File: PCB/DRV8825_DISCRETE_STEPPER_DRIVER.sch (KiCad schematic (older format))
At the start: 14 parts, among them U4 DRV8825PWPR

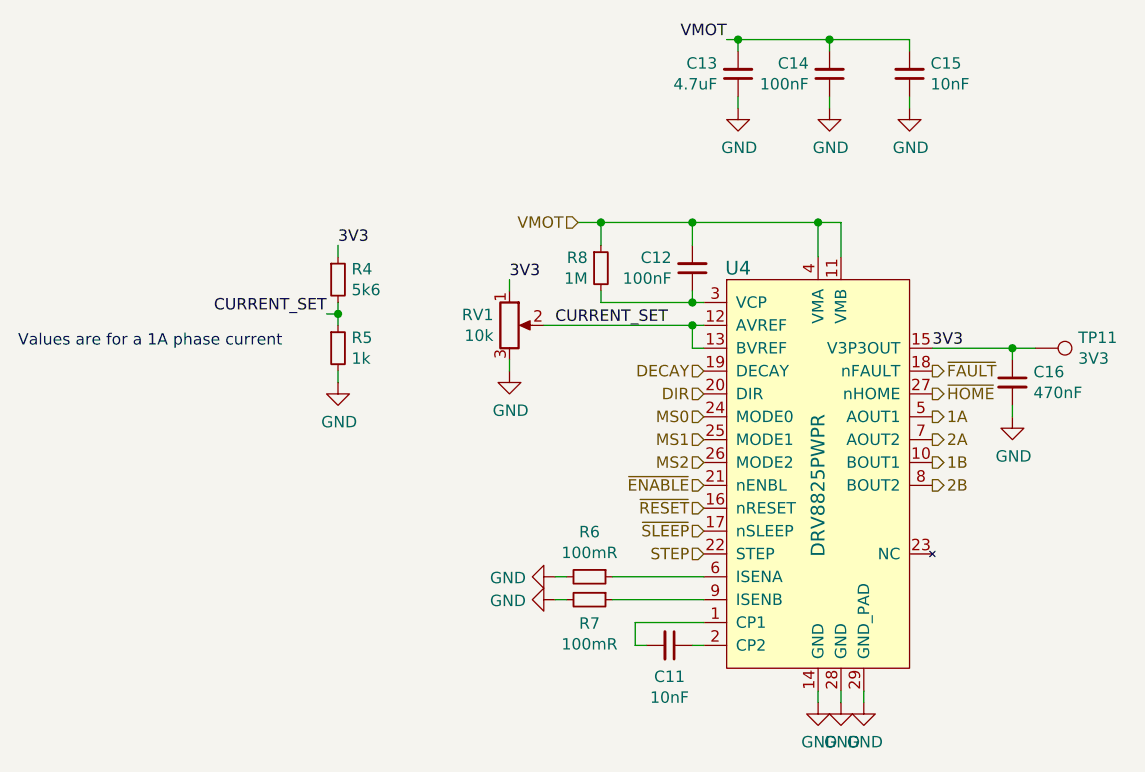
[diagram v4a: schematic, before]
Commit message: Added PDF schematic
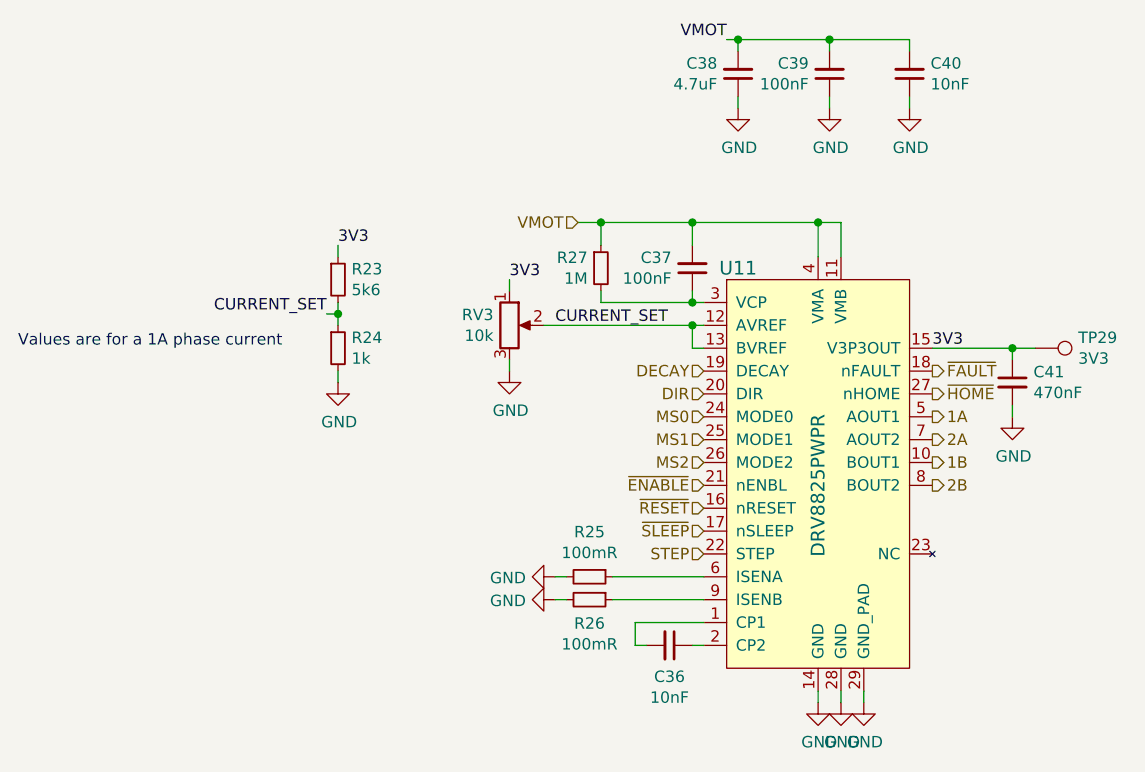
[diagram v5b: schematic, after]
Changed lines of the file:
@@
 AR Path="/5E8A6686/5E8D27A6/5E8D3351" Ref="U4"  Part="1"
 AR Path="/5E8813FF/5E8D27A6/5E8D3351" Ref="U11"  Part="1"
-F 0 "U4" H 5300 4500 60  0000 C CNN
+F 0 "U11" H 5300 4500 60  0000 C CNN
 F 1 "DRV8825PWPR" V 5650 3550 60  0000 C CNN
 F 2 "digikey-footprints:TSSOP-28-1EP_W4.40mm" H 5750 4050 60  0001 L CNN
@@
 AR Path="/5E8A6686/5E8D27A6/5E8D575F" Ref="C11"  Part="1"
 AR Path="/5E8813FF/5E8D27A6/5E8D575F" Ref="C36"  Part="1"
-F 0 "C11" V 5137 4850 50  0000 C CNN
+F 0 "C36" V 5137 4850 50  0000 C CNN
 F 1 "10nF" V 5228 4850 50  0000 C CNN
 F 2 "" H 5000 4850 50  0001 C CNN
@@
 AR Path="/5E8A6686/5E8D27A6/5E8D7A25" Ref="R6"  Part="1"
 AR Path="/5E8813FF/5E8D27A6/5E8D7A25" Ref="R25"  Part="1"
-F 0 "R6" V 4454 4550 50  0000 C CNN
+F 0 "R25" V 4454 4550 50  0000 C CNN
 F 1 "100mR" V 4545 4550 50  0000 C CNN
 F 2 "" H 4650 4550 50  0001 C CNN
@@
 AR Path="/5E8A6686/5E8D27A6/5E8D7F7E" Ref="R7"  Part="1"
 AR Path="/5E8813FF/5E8D27A6/5E8D7F7E" Ref="R26"  Part="1"
-F 0 "R7" V 4754 4650 50  0000 C CNN
+F 0 "R26" V 4754 4650 50  0000 C CNN
 F 1 "100mR" V 4845 4650 50  0000 C CNN
 F 2 "" H 4650 4650 50  0001 C CNN
@@
 AR Path="/5E8A6686/5E8D27A6/5E8D91C5" Ref="#PWR041"  Part="1"
 AR Path="/5E8813FF/5E8D27A6/5E8D91C5" Ref="#PWR0106"  Part="1"
-F 0 "#PWR041" H 4500 4300 50  0001 C CNN
+F 0 "#PWR0106" H 4500 4300 50  0001 C CNN
 F 1 "GND" V 4505 4422 50  0000 R CNN
 F 2 "" H 4500 4550 50  0001 C CNN
@@
 AR Path="/5E8A6686/5E8D27A6/5E8D92EE" Ref="#PWR042"  Part="1"
 AR Path="/5E8813FF/5E8D27A6/5E8D92EE" Ref="#PWR0107"  Part="1"
-F 0 "#PWR042" H 4500 4400 50  0001 C CNN
+F 0 "#PWR0107" H 4500 4400 50  0001 C CNN
 F 1 "GND" V 4505 4522 50  0000 R CNN
 F 2 "" H 4500 4650 50  0001 C CNN
@@
 AR Path="/5E8A6686/5E8D27A6/5E8DA337" Ref="C12"  Part="1"
 AR Path="/5E8813FF/5E8D27A6/5E8DA337" Ref="C37"  Part="1"
-F 0 "C12" H 5191 3154 50  0000 L CNN
+F 0 "C37" H 5191 3154 50  0000 L CNN
 F 1 "100nF" H 5191 3245 50  0000 L CNN
 F 2 "" H 5100 3200 50  0001 C CNN
@@
 AR Path="/5E8A6686/5E8D27A6/5E8DF1FC" Ref="RV1"  Part="1"
 AR Path="/5E8813FF/5E8D27A6/5E8DF1FC" Ref="RV3"  Part="1"
-F 0 "RV1" H 4230 3496 50  0000 R CNN
+F 0 "RV3" H 4230 3496 50  0000 R CNN
 F 1 "10k" H 4230 3405 50  0000 R CNN
 F 2 "" H 4300 3450 50  0001 C CNN
@@
 AR Path="/5E8A6686/5E8D27A6/5E8E02D7" Ref="#PWR040"  Part="1"
 AR Path="/5E8813FF/5E8D27A6/5E8E02D7" Ref="#PWR0105"  Part="1"
-F 0 "#PWR040" H 4300 3400 50  0001 C CNN
+F 0 "#PWR0105" H 4300 3400 50  0001 C CNN
 F 1 "GND" H 4305 3477 50  0000 C CNN
 F 2 "" H 4300 3650 50  0001 C CNN
@@
 AR Path="/5E8A6686/5E8D27A6/5E8E181B" Ref="C16"  Part="1"
 AR Path="/5E8813FF/5E8D27A6/5E8E181B" Ref="C41"  Part="1"
-F 0 "C16" H 6592 3746 50  0000 L CNN
+F 0 "C41" H 6592 3746 50  0000 L CNN
 F 1 "470nF" H 6592 3655 50  0000 L CNN
 F 2 "" H 6500 3700 50  0001 C CNN
@@
 AR Path="/5E8A6686/5E8D27A6/5E8E24E3" Ref="#PWR049"  Part="1"
 AR Path="/5E8813FF/5E8D27A6/5E8E24E3" Ref="#PWR0114"  Part="1"
-F 0 "#PWR049" H 6500 3600 50  0001 C CNN
+F 0 "#PWR0114" H 6500 3600 50  0001 C CNN
 F 1 "GND" H 6505 3677 50  0000 C CNN
 F 2 "" H 6500 3850 50  0001 C CNN
@@
 AR Path="/5E8A6686/5E8D27A6/5E8E69E3" Ref="#PWR044"  Part="1"
 AR Path="/5E8813FF/5E8D27A6/5E8E69E3" Ref="#PWR0109"  Part="1"
-F 0 "#PWR044" H 5650 4850 50  0001 C CNN
+F 0 "#PWR0109" H 5650 4850 50  0001 C CNN
 F 1 "GND" H 5655 4927 50  0000 C CNN
 F 2 "" H 5650 5100 50  0001 C CNN
@@
 AR Path="/5E8A6686/5E8D27A6/5E8E6E0E" Ref="#PWR046"  Part="1"
 AR Path="/5E8813FF/5E8D27A6/5E8E6E0E" Ref="#PWR0111"  Part="1"
-F 0 "#PWR046" H 5750 4850 50  0001 C CNN
+F 0 "#PWR0111" H 5750 4850 50  0001 C CNN
 F 1 "GND" H 5755 4927 50  0000 C CNN
 F 2 "" H 5750 5100 50  0001 C CNN
@@
 AR Path="/5E8A6686/5E8D27A6/5E8E6F63" Ref="#PWR047"  Part="1"
 AR Path="/5E8813FF/5E8D27A6/5E8E6F63" Ref="#PWR0112"  Part="1"
-F 0 "#PWR047" H 5850 4850 50  0001 C CNN
+F 0 "#PWR0112" H 5850 4850 50  0001 C CNN
 F 1 "GND" H 5855 4927 50  0000 C CNN
 F 2 "" H 5850 5100 50  0001 C CNN
@@
 AR Path="/5E8A6686/5E8D27A6/5E8E9760" Ref="C13"  Part="1"
 AR Path="/5E8813FF/5E8D27A6/5E8E9760" Ref="C38"  Part="1"
-F 0 "C13" H 5391 2304 50  0000 L CNN
+F 0 "C38" H 5391 2304 50  0000 L CNN
 F 1 "4.7uF" H 5391 2395 50  0000 L CNN
 F 2 "" H 5300 2350 50  0001 C CNN
@@
 AR Path="/5E8A6686/5E8D27A6/5E8E999E" Ref="C14"  Part="1"
 AR Path="/5E8813FF/5E8D27A6/5E8E999E" Ref="C39"  Part="1"
-F 0 "C14" H 5791 2304 50  0000 L CNN
+F 0 "C39" H 5791 2304 50  0000 L CNN
 F 1 "100nF" H 5791 2395 50  0000 L CNN
 F 2 "" H 5700 2350 50  0001 C CNN
@@
 AR Path="/5E8A6686/5E8D27A6/5E8E9DB5" Ref="C15"  Part="1"
 AR Path="/5E8813FF/5E8D27A6/5E8E9DB5" Ref="C40"  Part="1"
-F 0 "C15" H 5958 2304 50  0000 R CNN
+F 0 "C40" H 5958 2304 50  0000 R CNN
 F 1 "10nF" H 5958 2395 50  0000 R CNN
 F 2 "" H 6050 2350 50  0001 C CNN
@@
 AR Path="/5E8A6686/5E8D27A6/5E8F0245" Ref="#PWR043"  Part="1"
 AR Path="/5E8813FF/5E8D27A6/5E8F0245" Ref="#PWR0108"  Part="1"
-F 0 "#PWR043" H 5300 2250 50  0001 C CNN
+F 0 "#PWR0108" H 5300 2250 50  0001 C CNN
 F 1 "GND" H 5305 2327 50  0000 C CNN
 F 2 "" H 5300 2500 50  0001 C CNN
@@
 AR Path="/5E8A6686/5E8D27A6/5E8F04AF" Ref="#PWR045"  Part="1"
 AR Path="/5E8813FF/5E8D27A6/5E8F04AF" Ref="#PWR0110"  Part="1"
-F 0 "#PWR045" H 5700 2250 50  0001 C CNN
+F 0 "#PWR0110" H 5700 2250 50  0001 C CNN
 F 1 "GND" H 5705 2327 50  0000 C CNN
 F 2 "" H 5700 2500 50  0001 C CNN
@@
 AR Path="/5E8A6686/5E8D27A6/5E8F06A3" Ref="#PWR048"  Part="1"
 AR Path="/5E8813FF/5E8D27A6/5E8F06A3" Ref="#PWR0113"  Part="1"
-F 0 "#PWR048" H 6050 2250 50  0001 C CNN
+F 0 "#PWR0113" H 6050 2250 50  0001 C CNN
 F 1 "GND" H 6055 2327 50  0000 C CNN
 F 2 "" H 6050 2500 50  0001 C CNN
@@
 AR Path="/5E8A6686/5E8D27A6/5E8B797B" Ref="R4"  Part="1"
 AR Path="/5E8813FF/5E8D27A6/5E8B797B" Ref="R23"  Part="1"
-F 0 "R4" H 3609 3296 50  0000 L CNN
+F 0 "R23" H 3609 3296 50  0000 L CNN
 F 1 "5k6" H 3609 3205 50  0000 L CNN
 F 2 "" H 3550 3250 50  0001 C CNN
@@
 AR Path="/5E8A6686/5E8D27A6/5E8B7AF6" Ref="R5"  Part="1"
 AR Path="/5E8813FF/5E8D27A6/5E8B7AF6" Ref="R24"  Part="1"
-F 0 "R5" H 3609 3596 50  0000 L CNN
+F 0 "R24" H 3609 3596 50  0000 L CNN
 F 1 "1k" H 3609 3505 50  0000 L CNN
 F 2 "" H 3550 3550 50  0001 C CNN
@@
 AR Path="/5E8A6686/5E8D27A6/5E8B7CD9" Ref="#PWR039"  Part="1"
 AR Path="/5E8813FF/5E8D27A6/5E8B7CD9" Ref="#PWR0104"  Part="1"
-F 0 "#PWR039" H 3550 3450 50  0001 C CNN
+F 0 "#PWR0104" H 3550 3450 50  0001 C CNN
 F 1 "GND" H 3555 3527 50  0000 C CNN
 F 2 "" H 3550 3700 50  0001 C CNN
@@
 AR Path="/5E8A6686/5E8D27A6/5E8D6554" Ref="R8"  Part="1"
 AR Path="/5E8813FF/5E8D27A6/5E8D6554" Ref="R27"  Part="1"
-F 0 "R8" H 4642 3246 50  0000 R CNN
+F 0 "R27" H 4642 3246 50  0000 R CNN
 F 1 "1M" H 4642 3155 50  0000 R CNN
 F 2 "" H 4700 3200 50  0001 C CNN
@@
 AR Path="/5E8A6686/5E8D27A6/5E958C53" Ref="TP11"  Part="1"
 AR Path="/5E8813FF/5E8D27A6/5E958C53" Ref="TP29"  Part="1"
-F 0 "TP11" V 6554 3738 50  0000 L CNN
+F 0 "TP29" V 6554 3738 50  0000 L CNN
 F 1 "3V3" V 6645 3738 50  0000 L CNN
 F 2 "" H 6800 3550 50  0001 C CNN

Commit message: Added majority footprints
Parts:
- C11, C12, C13, C14, C15, C16: footprint (none) -> Capacitor_SMD:C_0603_1608Metric
- R4, R5, R8: footprint (none) -> Resistor_SMD:R_0603_1608Metric
- TP11: footprint (none) -> custom:TestPoint_Pad_D1.5mm
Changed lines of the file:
@@
 $Descr A4 11693 8268
 encoding utf-8
-Sheet 4 22
+Sheet 15 22
 Title ""
 Date ""
@@
 F 0 "C36" V 5137 4850 50  0000 C CNN
 F 1 "10nF" V 5228 4850 50  0000 C CNN
-F 2 "" H 5000 4850 50  0001 C CNN
+F 2 "Capacitor_SMD:C_0603_1608Metric" H 5000 4850 50  0001 C CNN
 F 3 "" H 5000 4850 50  0001 C CNN
 F 4 "X7R" H 5000 4850 50  0001 C CNN "Dielectric"
@@
 F 0 "C37" H 5191 3154 50  0000 L CNN
 F 1 "100nF" H 5191 3245 50  0000 L CNN
-F 2 "" H 5100 3200 50  0001 C CNN
+F 2 "Capacitor_SMD:C_0603_1608Metric" H 5100 3200 50  0001 C CNN
 F 3 "" H 5100 3200 50  0001 C CNN
 F 4 "X7R" H 5100 3200 50  0001 C CNN "Dielectric"
@@
 F 0 "C41" H 6592 3746 50  0000 L CNN
 F 1 "470nF" H 6592 3655 50  0000 L CNN
-F 2 "" H 6500 3700 50  0001 C CNN
+F 2 "Capacitor_SMD:C_0603_1608Metric" H 6500 3700 50  0001 C CNN
 F 3 "" H 6500 3700 50  0001 C CNN
 F 4 "X7R" H 6500 3700 50  0001 C CNN "Dielectric"
@@
 F 0 "C38" H 5391 2304 50  0000 L CNN
 F 1 "4.7uF" H 5391 2395 50  0000 L CNN
-F 2 "" H 5300 2350 50  0001 C CNN
+F 2 "Capacitor_SMD:C_0603_1608Metric" H 5300 2350 50  0001 C CNN
 F 3 "" H 5300 2350 50  0001 C CNN
 F 4 "50V" H 5300 2350 50  0001 C CNN "Voltage Rating"
@@
 F 0 "C39" H 5791 2304 50  0000 L CNN
 F 1 "100nF" H 5791 2395 50  0000 L CNN
-F 2 "" H 5700 2350 50  0001 C CNN
+F 2 "Capacitor_SMD:C_0603_1608Metric" H 5700 2350 50  0001 C CNN
 F 3 "" H 5700 2350 50  0001 C CNN
 F 4 "50V" H 5700 2350 50  0001 C CNN "Voltage Rating"
@@
 F 0 "C40" H 5958 2304 50  0000 R CNN
 F 1 "10nF" H 5958 2395 50  0000 R CNN
-F 2 "" H 6050 2350 50  0001 C CNN
+F 2 "Capacitor_SMD:C_0603_1608Metric" H 6050 2350 50  0001 C CNN
 F 3 "" H 6050 2350 50  0001 C CNN
 F 4 "50V" H 6050 2350 50  0001 C CNN "Voltage Rating"
@@
 F 0 "R23" H 3609 3296 50  0000 L CNN
 F 1 "5k6" H 3609 3205 50  0000 L CNN
-F 2 "" H 3550 3250 50  0001 C CNN
+F 2 "Resistor_SMD:R_0603_1608Metric" H 3550 3250 50  0001 C CNN
 F 3 "" H 3550 3250 50  0001 C CNN
 	1    3550 3250
@@
 F 0 "R24" H 3609 3596 50  0000 L CNN
 F 1 "1k" H 3609 3505 50  0000 L CNN
-F 2 "" H 3550 3550 50  0001 C CNN
+F 2 "Resistor_SMD:R_0603_1608Metric" H 3550 3550 50  0001 C CNN
 F 3 "" H 3550 3550 50  0001 C CNN
 	1    3550 3550
@@
 F 0 "R27" H 4642 3246 50  0000 R CNN
 F 1 "1M" H 4642 3155 50  0000 R CNN
-F 2 "" H 4700 3200 50  0001 C CNN
+F 2 "Resistor_SMD:R_0603_1608Metric" H 4700 3200 50  0001 C CNN
 F 3 "" H 4700 3200 50  0001 C CNN
 	1    4700 3200
@@
 F 0 "TP29" V 6554 3738 50  0000 L CNN
 F 1 "3V3" V 6645 3738 50  0000 L CNN
-F 2 "" H 6800 3550 50  0001 C CNN
+F 2 "custom:TestPoint_Pad_D1.5mm" H 6800 3550 50  0001 C CNN
 F 3 "~" H 6800 3550 50  0001 C CNN
 	1    6600 3550

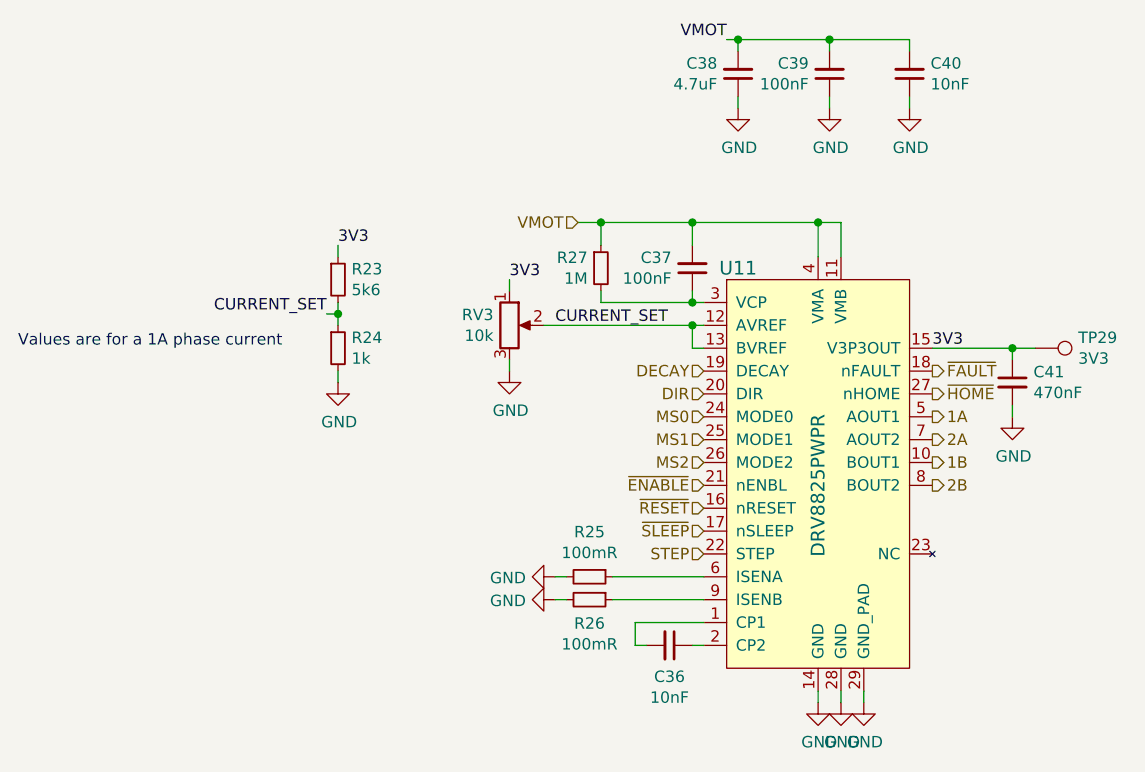
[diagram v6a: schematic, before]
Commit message: Added more footprints
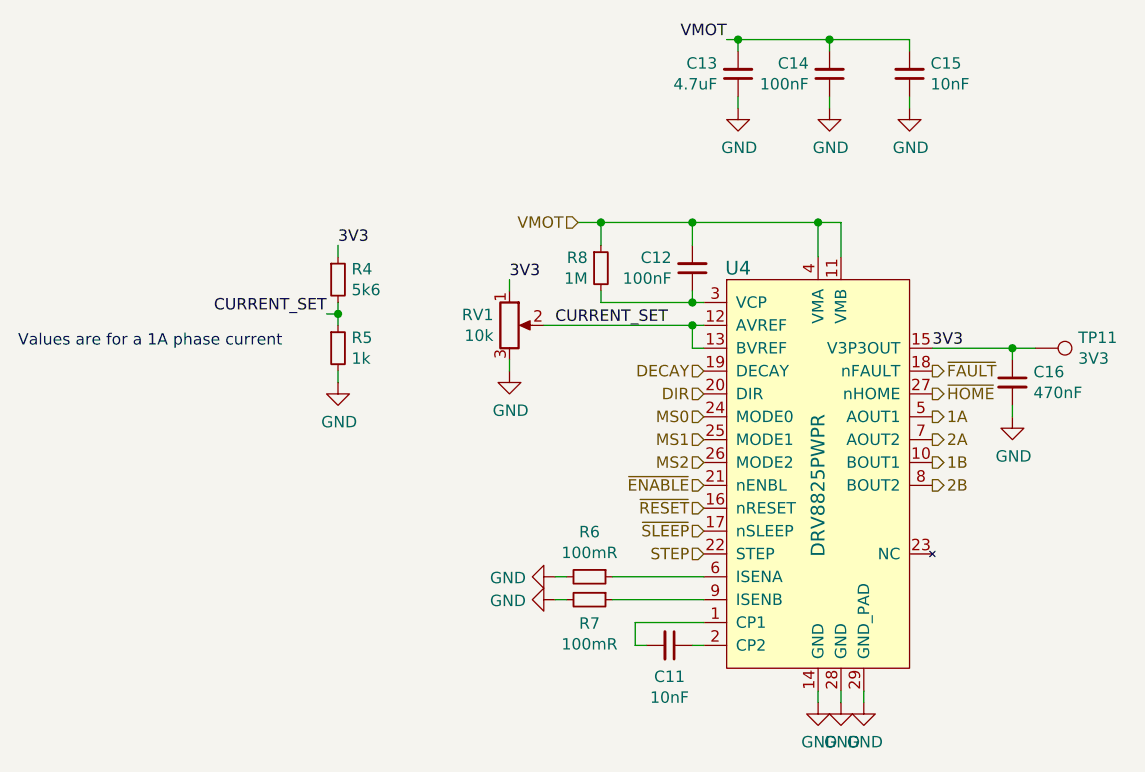
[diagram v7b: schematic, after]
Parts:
- RV1: footprint (none) -> Resistors:TRIMPOT-SMD-TC33X; MPN (none) -> TC33X-2-103E
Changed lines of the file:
@@
 $Descr A4 11693 8268
 encoding utf-8
-Sheet 15 22
+Sheet 4 22
 Title ""
 Date ""
@@
 AR Path="/5E8A6686/5E8D27A6/5E8D3351" Ref="U4"  Part="1"
 AR Path="/5E8813FF/5E8D27A6/5E8D3351" Ref="U11"  Part="1"
-F 0 "U11" H 5300 4500 60  0000 C CNN
+F 0 "U4" H 5300 4500 60  0000 C CNN
 F 1 "DRV8825PWPR" V 5650 3550 60  0000 C CNN
 F 2 "digikey-footprints:TSSOP-28-1EP_W4.40mm" H 5750 4050 60  0001 L CNN
@@
 AR Path="/5E8A6686/5E8D27A6/5E8D575F" Ref="C11"  Part="1"
 AR Path="/5E8813FF/5E8D27A6/5E8D575F" Ref="C36"  Part="1"
-F 0 "C36" V 5137 4850 50  0000 C CNN
+F 0 "C11" V 5137 4850 50  0000 C CNN
 F 1 "10nF" V 5228 4850 50  0000 C CNN
 F 2 "Capacitor_SMD:C_0603_1608Metric" H 5000 4850 50  0001 C CNN
@@
 AR Path="/5E8A6686/5E8D27A6/5E8D7A25" Ref="R6"  Part="1"
 AR Path="/5E8813FF/5E8D27A6/5E8D7A25" Ref="R25"  Part="1"
-F 0 "R25" V 4454 4550 50  0000 C CNN
+F 0 "R6" V 4454 4550 50  0000 C CNN
 F 1 "100mR" V 4545 4550 50  0000 C CNN
 F 2 "" H 4650 4550 50  0001 C CNN
@@
 AR Path="/5E8A6686/5E8D27A6/5E8D7F7E" Ref="R7"  Part="1"
 AR Path="/5E8813FF/5E8D27A6/5E8D7F7E" Ref="R26"  Part="1"
-F 0 "R26" V 4754 4650 50  0000 C CNN
+F 0 "R7" V 4754 4650 50  0000 C CNN
 F 1 "100mR" V 4845 4650 50  0000 C CNN
 F 2 "" H 4650 4650 50  0001 C CNN
@@
 AR Path="/5E8A6686/5E8D27A6/5E8DA337" Ref="C12"  Part="1"
 AR Path="/5E8813FF/5E8D27A6/5E8DA337" Ref="C37"  Part="1"
-F 0 "C37" H 5191 3154 50  0000 L CNN
+F 0 "C12" H 5191 3154 50  0000 L CNN
 F 1 "100nF" H 5191 3245 50  0000 L CNN
 F 2 "Capacitor_SMD:C_0603_1608Metric" H 5100 3200 50  0001 C CNN
@@
 AR Path="/5E8A6686/5E8D27A6/5E8DF1FC" Ref="RV1"  Part="1"
 AR Path="/5E8813FF/5E8D27A6/5E8DF1FC" Ref="RV3"  Part="1"
-F 0 "RV3" H 4230 3496 50  0000 R CNN
+F 0 "RV1" H 4230 3496 50  0000 R CNN
 F 1 "10k" H 4230 3405 50  0000 R CNN
-F 2 "" H 4300 3450 50  0001 C CNN
+F 2 "Resistors:TRIMPOT-SMD-TC33X" H 4300 3450 50  0001 C CNN
 F 3 "" H 4300 3450 50  0001 C CNN
+F 4 "TC33X-2-103E" H 4300 3450 50  0001 C CNN "MPN"
 	1    4300 3450
 	1    0    0    -1
@@
 AR Path="/5E8A6686/5E8D27A6/5E8E181B" Ref="C16"  Part="1"
 AR Path="/5E8813FF/5E8D27A6/5E8E181B" Ref="C41"  Part="1"
-F 0 "C41" H 6592 3746 50  0000 L CNN
+F 0 "C16" H 6592 3746 50  0000 L CNN
 F 1 "470nF" H 6592 3655 50  0000 L CNN
 F 2 "Capacitor_SMD:C_0603_1608Metric" H 6500 3700 50  0001 C CNN
@@
 AR Path="/5E8A6686/5E8D27A6/5E8E9760" Ref="C13"  Part="1"
 AR Path="/5E8813FF/5E8D27A6/5E8E9760" Ref="C38"  Part="1"
-F 0 "C38" H 5391 2304 50  0000 L CNN
+F 0 "C13" H 5391 2304 50  0000 L CNN
 F 1 "4.7uF" H 5391 2395 50  0000 L CNN
 F 2 "Capacitor_SMD:C_0603_1608Metric" H 5300 2350 50  0001 C CNN
@@
 AR Path="/5E8A6686/5E8D27A6/5E8E999E" Ref="C14"  Part="1"
 AR Path="/5E8813FF/5E8D27A6/5E8E999E" Ref="C39"  Part="1"
-F 0 "C39" H 5791 2304 50  0000 L CNN
+F 0 "C14" H 5791 2304 50  0000 L CNN
 F 1 "100nF" H 5791 2395 50  0000 L CNN
 F 2 "Capacitor_SMD:C_0603_1608Metric" H 5700 2350 50  0001 C CNN
@@
 AR Path="/5E8A6686/5E8D27A6/5E8E9DB5" Ref="C15"  Part="1"
 AR Path="/5E8813FF/5E8D27A6/5E8E9DB5" Ref="C40"  Part="1"
-F 0 "C40" H 5958 2304 50  0000 R CNN
+F 0 "C15" H 5958 2304 50  0000 R CNN
 F 1 "10nF" H 5958 2395 50  0000 R CNN
 F 2 "Capacitor_SMD:C_0603_1608Metric" H 6050 2350 50  0001 C CNN
@@
 AR Path="/5E8A6686/5E8D27A6/5E8B797B" Ref="R4"  Part="1"
 AR Path="/5E8813FF/5E8D27A6/5E8B797B" Ref="R23"  Part="1"
-F 0 "R23" H 3609 3296 50  0000 L CNN
+F 0 "R4" H 3609 3296 50  0000 L CNN
 F 1 "5k6" H 3609 3205 50  0000 L CNN
 F 2 "Resistor_SMD:R_0603_1608Metric" H 3550 3250 50  0001 C CNN
@@
 AR Path="/5E8A6686/5E8D27A6/5E8B7AF6" Ref="R5"  Part="1"
 AR Path="/5E8813FF/5E8D27A6/5E8B7AF6" Ref="R24"  Part="1"
-F 0 "R24" H 3609 3596 50  0000 L CNN
+F 0 "R5" H 3609 3596 50  0000 L CNN
 F 1 "1k" H 3609 3505 50  0000 L CNN
 F 2 "Resistor_SMD:R_0603_1608Metric" H 3550 3550 50  0001 C CNN
@@
 AR Path="/5E8A6686/5E8D27A6/5E8D6554" Ref="R8"  Part="1"
 AR Path="/5E8813FF/5E8D27A6/5E8D6554" Ref="R27"  Part="1"
-F 0 "R27" H 4642 3246 50  0000 R CNN
+F 0 "R8" H 4642 3246 50  0000 R CNN
 F 1 "1M" H 4642 3155 50  0000 R CNN
 F 2 "Resistor_SMD:R_0603_1608Metric" H 4700 3200 50  0001 C CNN
@@
 AR Path="/5E8A6686/5E8D27A6/5E958C53" Ref="TP11"  Part="1"
 AR Path="/5E8813FF/5E8D27A6/5E958C53" Ref="TP29"  Part="1"
-F 0 "TP29" V 6554 3738 50  0000 L CNN
+F 0 "TP11" V 6554 3738 50  0000 L CNN
 F 1 "3V3" V 6645 3738 50  0000 L CNN
 F 2 "custom:TestPoint_Pad_D1.5mm" H 6800 3550 50  0001 C CNN
